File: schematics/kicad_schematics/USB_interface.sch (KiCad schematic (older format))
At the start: 13 parts, among them Q1 NPN-SC-59, Q2 NPN-SC-59, U8 USB-MINI-B-SHELL, U9 USBLC6-2P6

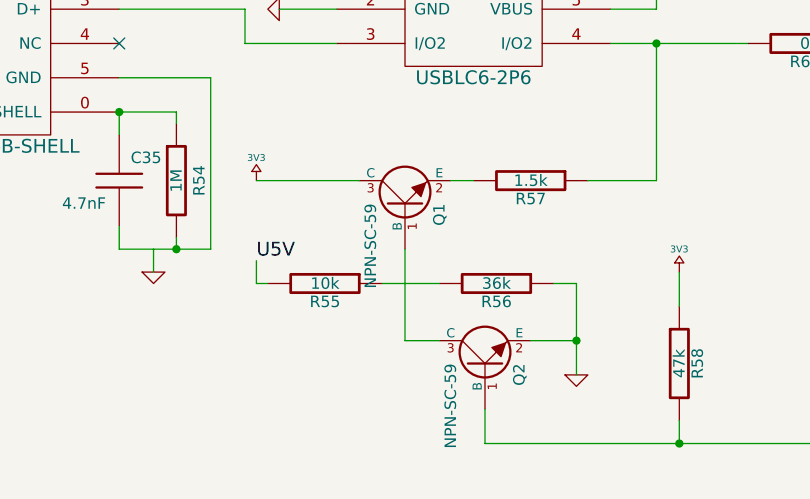
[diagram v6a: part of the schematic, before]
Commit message: modified SM0603 and schematics, along with lots of work done on PCB layout design
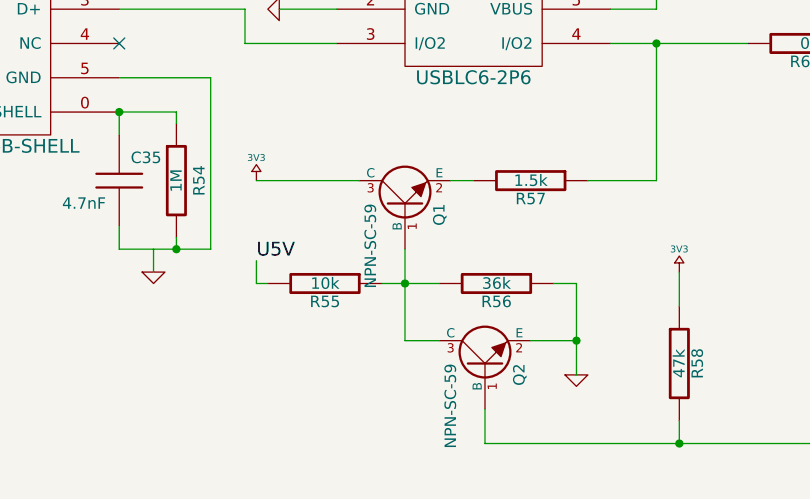
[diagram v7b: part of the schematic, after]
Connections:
- net at R55.1, R56.2: now also Q1.1 (B), Q2.3 (C)
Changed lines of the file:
@@
-EESchema Schematic File Version 2  date Tue 16 Mar 2010 05:07:11 PM EDT
+EESchema Schematic File Version 2  date Tue 16 Mar 2010 10:34:52 PM EDT
 LIBS:power
 LIBS:device
@@
 Sheet 5 5
 Title ""
-Date "16 mar 2010"
+Date "17 mar 2010"
 Rev ""
 Comp ""
@@
 Comment4 ""
 $EndDescr
+Wire Wire Line
+	4650 4400 4900 4400
+Connection ~ 5850 2450
+Wire Wire Line
+	6150 2300 5850 2300
+Wire Wire Line
+	5850 2300 5850 3200
+Wire Wire Line
+	3500 3750 3500 3650
+Wire Wire Line
+	3650 4250 3650 4350
+Connection ~ 3550 2900
+Wire Wire Line
+	3550 2900 3550 2550
+Wire Wire Line
+	3550 2550 3300 2550
+Connection ~ 5950 5100
+Wire Wire Line
+	5950 5000 5950 5100
+Connection ~ 5500 4650
+Wire Wire Line
+	4900 4650 4750 4650
+Wire Wire Line
+	4750 4650 4750 4250
+Wire Wire Line
+	4150 4400 4100 4400
+Wire Wire Line
+	4100 4400 4100 4300
+Wire Wire Line
+	5050 3950 4950 3950
+Wire Wire Line
+	6150 2850 6150 2950
+Wire Wire Line
+	6750 3350 7450 3350
+Wire Wire Line
+	5650 3350 6250 3350
+Wire Wire Line
+	3900 2900 3500 2900
+Wire Wire Line
+	4450 3050 3500 3050
+Connection ~ 3500 3650
+Wire Wire Line
+	3750 3700 3750 3650
+Wire Wire Line
+	3750 3650 3500 3650
+Wire Wire Line
+	3750 4200 3750 4250
+Wire Wire Line
+	3500 4150 3500 4250
+Wire Wire Line
+	4450 3200 4200 3200
+Wire Wire Line
+	3500 3200 4050 3200
+Wire Wire Line
+	4050 3200 4050 3350
+Wire Wire Line
+	4050 3350 4450 3350
+Wire Wire Line
+	5850 3200 5650 3200
+Wire Wire Line
+	6250 3050 5650 3050
+Wire Wire Line
+	7450 3050 6750 3050
+Wire Wire Line
+	5850 2450 6150 2450
+Wire Wire Line
+	5550 3950 5850 3950
+Wire Wire Line
+	5850 3950 5850 3350
+Connection ~ 5850 3350
+Wire Wire Line
+	4100 3950 4550 3950
+Wire Wire Line
+	5400 4400 5500 4400
+Wire Wire Line
+	5500 4400 5500 4800
+Wire Wire Line
+	5300 4650 5500 4650
+Wire Wire Line
+	5100 4950 5100 5100
+Wire Wire Line
+	5100 5100 6600 5100
+Wire Wire Line
+	5950 4500 5950 4350
+Wire Wire Line
+	3500 4250 3900 4250
+Connection ~ 3750 4250
+Wire Wire Line
+	3500 3500 3900 3500
+Wire Wire Line
+	3900 3500 3900 4250
+Connection ~ 4750 4400
 $Comp
 L GND #PWR073
@@
 Text Label 6150 2300 2    60   ~ 0
 U5V
-Connection ~ 5850 2450
-Wire Wire Line
-	6150 2300 5850 2300
-Wire Wire Line
-	5850 2300 5850 3200
-Wire Wire Line
-	3500 3750 3500 3650
-Wire Wire Line
-	3650 4250 3650 4350
-Connection ~ 3550 2900
-Wire Wire Line
-	3550 2900 3550 2550
-Wire Wire Line
-	3550 2550 3300 2550
-Connection ~ 5950 5100
-Wire Wire Line
-	5950 5000 5950 5100
-Connection ~ 5500 4650
-Wire Wire Line
-	4900 4650 4750 4650
-Wire Wire Line
-	4750 4650 4750 4250
-Wire Wire Line
-	4150 4400 4100 4400
-Wire Wire Line
-	4100 4400 4100 4300
-Wire Wire Line
-	5050 3950 4950 3950
-Wire Wire Line
-	6150 2850 6150 2950
-Wire Wire Line
-	6750 3350 7450 3350
-Wire Wire Line
-	5650 3350 6250 3350
-Wire Wire Line
-	3900 2900 3500 2900
-Wire Wire Line
-	4450 3050 3500 3050
-Connection ~ 3500 3650
-Wire Wire Line
-	3750 3700 3750 3650
-Wire Wire Line
-	3750 3650 3500 3650
-Wire Wire Line
-	3750 4200 3750 4250
-Wire Wire Line
-	3500 4150 3500 4250
-Wire Wire Line
-	4450 3200 4200 3200
-Wire Wire Line
-	3500 3200 4050 3200
-Wire Wire Line
-	4050 3200 4050 3350
-Wire Wire Line
-	4050 3350 4450 3350
-Wire Wire Line
-	5850 3200 5650 3200
-Wire Wire Line
-	6250 3050 5650 3050
-Wire Wire Line
-	7450 3050 6750 3050
-Wire Wire Line
-	5850 2450 6150 2450
-Wire Wire Line
-	5550 3950 5850 3950
-Wire Wire Line
-	5850 3950 5850 3350
-Connection ~ 5850 3350
-Wire Wire Line
-	4100 3950 4550 3950
-Wire Wire Line
-	4650 4400 4900 4400
-Wire Wire Line
-	5400 4400 5500 4400
-Wire Wire Line
-	5500 4400 5500 4800
-Wire Wire Line
-	5300 4650 5500 4650
-Wire Wire Line
-	5100 4950 5100 5100
-Wire Wire Line
-	5100 5100 6600 5100
-Wire Wire Line
-	5950 4500 5950 4350
-Wire Wire Line
-	3500 4250 3900 4250
-Connection ~ 3750 4250
-Wire Wire Line
-	3500 3500 3900 3500
-Wire Wire Line
-	3900 3500 3900 4250
 Text Label 3900 2900 2    60   ~ 0
 U5V

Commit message: made some major changes to the PCB layout
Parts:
- Q1, Q2: footprint -SOT23 -> SOT23
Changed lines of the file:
@@
-EESchema Schematic File Version 2  date Tue 16 Mar 2010 10:34:52 PM EDT
+EESchema Schematic File Version 2  date Wed 17 Mar 2010 01:46:08 PM EDT
 LIBS:power
 LIBS:device
@@
 F 0 "Q2" H 5100 4600 50  0000 R CNN
 F 1 "NPN-SC-59" H 5100 4900 50  0000 R CNN
-F 2 "-SOT23" H 5100 4750 60  0001 C CNN
+F 2 "SOT23" H 5100 4750 60  0001 C CNN
 	1    5100 4750
 	0    -1   -1   0
@@
 F 0 "Q1" H 4750 3900 50  0000 R CNN
 F 1 "NPN-SC-59" H 4750 4200 50  0000 R CNN
-F 2 "-SOT23" H 4750 4050 60  0001 C CNN
+F 2 "SOT23" H 4750 4050 60  0001 C CNN
 	1    4750 4050
 	0    -1   -1   0
